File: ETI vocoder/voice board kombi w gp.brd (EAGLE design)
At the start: 160 x 60.3 mm, 174 parts, among them IC1 TL072P, IC1. TL072P, IC2 TL072P, IC2. TL072P, IC3 TL081P, IC3. TL081P, IC4 TL081P, IC4. TL081P, IC5 TL072P, IC6 LM13600AN, IC7 TL072P, IC7. TL072P, P1 C-OR-R050_075-025X100, P1. C-OR-R050_075-025X100, P10 C-OR-R050_075-025X100, P10. C-OR-R050_075-025X100, P11 C-OR-R050_075-025X100, P11. C-OR-R050_075-025X100, P12 C-OR-R050_075-025X100, P12. C-OR-R050_075-025X100, P13 C-OR-R050_075-025X100, P13. C-OR-R050_075-025X100, P14 C-OR-R050_075-025X100, P14. C-OR-R050_075-025X100, P15 C-OR-R050_075-025X100, P15. C-OR-R050_075-025X100, P16 C-OR-R050_075-025X100, P16. C-OR-R050_075-025X100, P2 C-OR-R050_075-025X100, P2. C-OR-R050_075-025X100, P3 C-OR-R050_075-025X100, P3. C-OR-R050_075-025X100, P4 C-OR-R050_075-025X100, P4. C-OR-R050_075-025X100, P5 C-OR-R050_075-025X100, P5. C-OR-R050_075-025X100, P6 C-OR-R050_075-025X100, P6. C-OR-R050_075-025X100, P7 C-OR-R050_075-025X100, P7. C-OR-R050_075-025X100, P8 C-OR-R050_075-025X100, P8. C-OR-R050_075-025X100, P9 C-OR-R050_075-025X100, P9. C-OR-R050_075-025X100, Q1 BF244C, Q1. BF244C, Q2 BC212L, Q2. BC212L

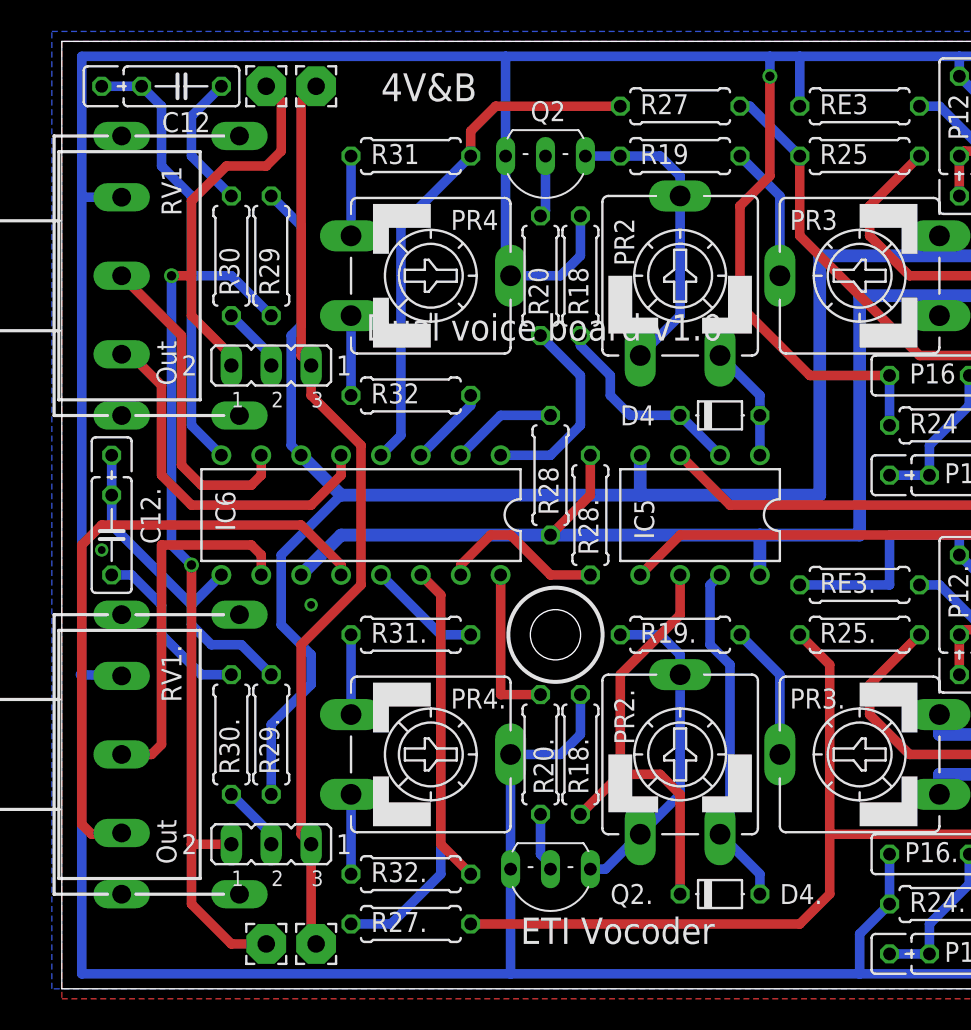
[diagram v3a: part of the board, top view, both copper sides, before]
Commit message: Added place to write channel numbers
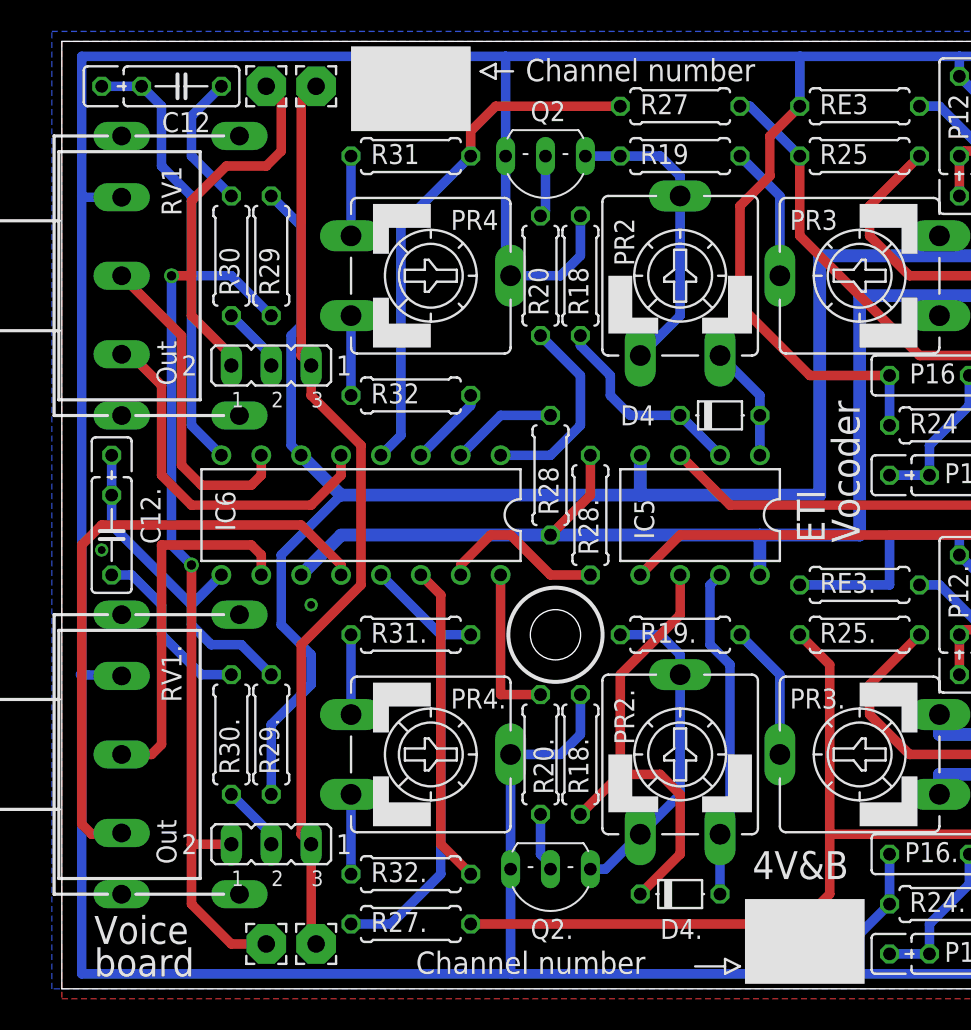
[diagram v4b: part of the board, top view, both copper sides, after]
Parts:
- moved D4. 2.54 mm to (39.4, 6.03)
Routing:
- net GND: track 817.3 -> 814.9 mm, vias 5 -> 4
- net N$68: track 22.4 -> 21.4 mm
- net N$67: track 28.6 -> 29.6 mm
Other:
- board text added: "Channel number"
- board text added: "ETI"
- board text added: "Vocoder"
- board text added: "Voice"
- board text added: "board"
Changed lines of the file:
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@@
 <setting verticaltext="up"/>
 </settings>
-<grid distance="0.0125" unitdist="inch" unit="inch" style="dots" multiple="1" display="yes" altdistance="0.025" altunitdist="inch" altunit="inch"/>
+<grid distance="0.00625" unitdist="inch" unit="inch" style="dots" multiple="1" display="yes" altdistance="0.025" altunitdist="inch" altunit="inch"/>
 <layers>
 <layer number="1" name="Top" color="4" fill="1" visible="yes" active="yes"/>
@@
 <hole x="156.21" y="7.9375" drill="3.2"/>
 <circle x="156.21" y="7.9375" radius="3" width="0.254" layer="25"/>
-<text x="20.32" y="56.515" size="1.778" layer="25" font="vector">4V&amp;B</text>
-<text x="19.3675" y="41.275" size="1.6764" layer="25" font="vector">Dual voice board v1.0</text>
-<text x="29.21" y="2.8575" size="1.6764" layer="25" font="vector">ETI Vocoder</text>
+<text x="43.97375" y="6.985" size="1.778" layer="25" font="vector">4V&amp;B</text>
 <text x="95.25" y="55.5625" size="1.27" layer="26" font="vector" rot="MR270">Slew</text>
 <text x="98.425" y="55.5625" size="1.27" layer="26" font="vector" rot="MR270">V/UV</text>
@@
 <rectangle x1="135.4455" y1="41.91" x2="139.5095" y2="42.037" layer="26"/>
 <rectangle x1="136.2075" y1="42.037" x2="138.7475" y2="42.164" layer="26"/>
+<rectangle x1="18.415" y1="54.61" x2="26.035" y2="60.0075" layer="25"/>
+<text x="29.5275" y="57.785" size="1.4224" layer="25">Channel number</text>
+<wire x1="28.73375" y1="58.42" x2="27.6225" y2="58.42" width="0.15" layer="25"/>
+<wire x1="27.6225" y1="58.42" x2="27.6225" y2="58.89625" width="0.15" layer="25"/>
+<wire x1="27.6225" y1="58.89625" x2="26.67" y2="58.42" width="0.15" layer="25"/>
+<wire x1="26.67" y1="58.42" x2="27.6225" y2="57.94375" width="0.15" layer="25"/>
+<wire x1="27.6225" y1="57.94375" x2="27.6225" y2="58.42" width="0.15" layer="25"/>
+<rectangle x1="43.4975" y1="0.3175" x2="51.1175" y2="5.715" layer="25"/>
+<text x="22.5425" y="0.9525" size="1.4224" layer="25">Channel number</text>
+<wire x1="40.3225" y1="1.42875" x2="42.2275" y2="1.42875" width="0.15" layer="25"/>
+<wire x1="42.2275" y1="1.42875" x2="42.2275" y2="1.905" width="0.15" layer="25"/>
+<wire x1="42.2275" y1="1.905" x2="43.18" y2="1.42875" width="0.15" layer="25"/>
+<wire x1="43.18" y1="1.42875" x2="42.2275" y2="0.9525" width="0.15" layer="25"/>
+<wire x1="42.2275" y1="0.9525" x2="42.2275" y2="1.42875" width="0.15" layer="25"/>
+<text x="2.06375" y="2.8575" size="1.778" layer="25">Voice</text>
+<text x="2.06375" y="0.79375" size="1.778" layer="25">board</text>
+<text x="48.5775" y="28.41625" size="1.778" layer="25" rot="R90">ETI</text>
+<text x="50.8" y="28.41625" size="1.778" layer="25" rot="R90">Vocoder</text>
+<text x="153.035" y="23.33625" size="1.27" layer="26" rot="MR270">ETI Vocoder</text>
+<text x="153.82875" y="48.10125" size="1.27" layer="26" rot="MR270">Dual voice
+board v1.0</text>
 </plain>
 <attributes>
@@
 <attribute name="VALUE" x="33.5788" y="12.6365" size="1.27" layer="27" ratio="10" rot="R90"/>
 </element>
-<element name="D4." library="diode" package="D-5" value="" x="41.91" y="6.0325" smashed="yes">
-<attribute name="NAME" x="45.72" y="5.3975" size="1.27" layer="25" ratio="10"/>
-<attribute name="VALUE" x="40.005" y="3.4925" size="1.27" layer="27" ratio="10"/>
+<element name="D4." library="diode" package="D-5" value="" x="39.37" y="6.0325" smashed="yes">
+<attribute name="NAME" x="38.1" y="3.175" size="1.27" layer="25" ratio="10"/>
+<attribute name="VALUE" x="37.465" y="3.4925" size="1.27" layer="27" ratio="10"/>
 </element>
 <element name="PR2." library="pot" package="CA9V" value="" x="39.37" y="14.9225" smashed="yes">
@@
 </element>
 <element name="Q2." library="transistor-neu-to92" package="TO92-ECB" value="BC212L" x="31.115" y="7.62" smashed="yes" rot="R180">
-<attribute name="NAME" x="34.925" y="5.3975" size="1.27" layer="25" ratio="10"/>
+<attribute name="NAME" x="29.845" y="3.175" size="1.27" layer="25" ratio="10"/>
 <attribute name="VALUE" x="27.94" y="8.89" size="1.27" layer="27" ratio="10" rot="R180"/>
 </element>
@@
 <wire x1="33.02" y1="46.6725" x2="33.02" y2="49.2125" width="0.6096" layer="16"/>
 <wire x1="28.2575" y1="53.0225" x2="28.2575" y2="59.3725" width="0.6096" layer="16"/>
-<wire x1="28.2575" y1="59.3725" x2="45.085" y2="59.3725" width="0.6096" layer="16"/>
-<wire x1="45.085" y1="59.3725" x2="46.99" y2="59.3725" width="0.6096" layer="16"/>
+<wire x1="28.2575" y1="59.3725" x2="46.99" y2="59.3725" width="0.6096" layer="16"/>
 <wire x1="46.99" y1="59.3725" x2="57.15" y2="59.3725" width="0.6096" layer="16"/>
 <wire x1="52.705" y1="39.0525" x2="52.705" y2="35.8775" width="0.6096" layer="16"/>
@@
 <wire x1="43.18" y1="43.4975" x2="43.18" y2="49.8475" width="0.6096" layer="1"/>
 <wire x1="43.18" y1="49.8475" x2="45.085" y2="51.7525" width="0.6096" layer="1"/>
-<wire x1="45.085" y1="51.7525" x2="45.085" y2="58.1025" width="0.6096" layer="1"/>
-<via x="45.085" y="58.1025" extent="1-16" drill="0.6"/>
-<wire x1="45.085" y1="58.1025" x2="45.085" y2="59.3725" width="0.6096" layer="16"/>
+<wire x1="45.085" y1="51.7525" x2="45.085" y2="54.2925" width="0.6096" layer="1"/>
 <wire x1="46.99" y1="56.1975" x2="46.99" y2="59.3725" width="0.6096" layer="16"/>
 <wire x1="60.325" y1="54.9275" x2="57.15" y2="58.1025" width="0.6096" layer="16"/>
@@
 <via x="2.54" y="27.94" extent="1-16" drill="0.5"/>
 <via x="135.5725" y="53.34" extent="1-16" drill="0.5"/>
+<wire x1="45.085" y1="54.2925" x2="46.99" y2="56.1975" width="0.6096" layer="1"/>
 </signal>
 <signal name="N$5">
@@
 <wire x1="35.56" y1="20.0025" x2="35.56" y2="13.6525" width="0.6096" layer="1"/>
 <wire x1="35.56" y1="13.6525" x2="33.02" y2="11.1125" width="0.6096" layer="1"/>
-<wire x1="39.37" y1="6.0325" x2="39.37" y2="12.3825" width="0.6096" layer="1"/>
+<wire x1="36.83" y1="6.0325" x2="39.37" y2="8.5725" width="0.6096" layer="1"/>
+<wire x1="39.37" y1="8.5725" x2="39.37" y2="12.3825" width="0.6096" layer="1"/>
 <wire x1="39.37" y1="12.3825" x2="38.1" y2="13.6525" width="0.6096" layer="1"/>
 <wire x1="38.1" y1="13.6525" x2="35.56" y2="13.6525" width="0.6096" layer="1"/>
@@
 <wire x1="42.545" y1="20.6375" x2="42.545" y2="10.4775" width="0.6096" layer="16"/>
 <wire x1="42.545" y1="10.4775" x2="41.91" y2="9.8425" width="0.6096" layer="16"/>
-<wire x1="44.45" y1="6.0325" x2="44.45" y2="7.3025" width="0.6096" layer="16"/>
-<wire x1="44.45" y1="7.3025" x2="41.91" y2="9.8425" width="0.6096" layer="16"/>
+<wire x1="41.91" y1="6.0325" x2="41.91" y2="9.8425" width="0.6096" layer="16"/>
 </signal>
 <signal name="N$69">
